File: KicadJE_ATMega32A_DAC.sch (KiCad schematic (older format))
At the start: 72 parts, among them J201 CV1, J202 CV2, J203 OUT1, J204 OUT2, J205 IN1, J206 IN2, P201 Doepfer_Power_16pin, SW201 SW_SPDT, U201 TL072, U202 MCP4822

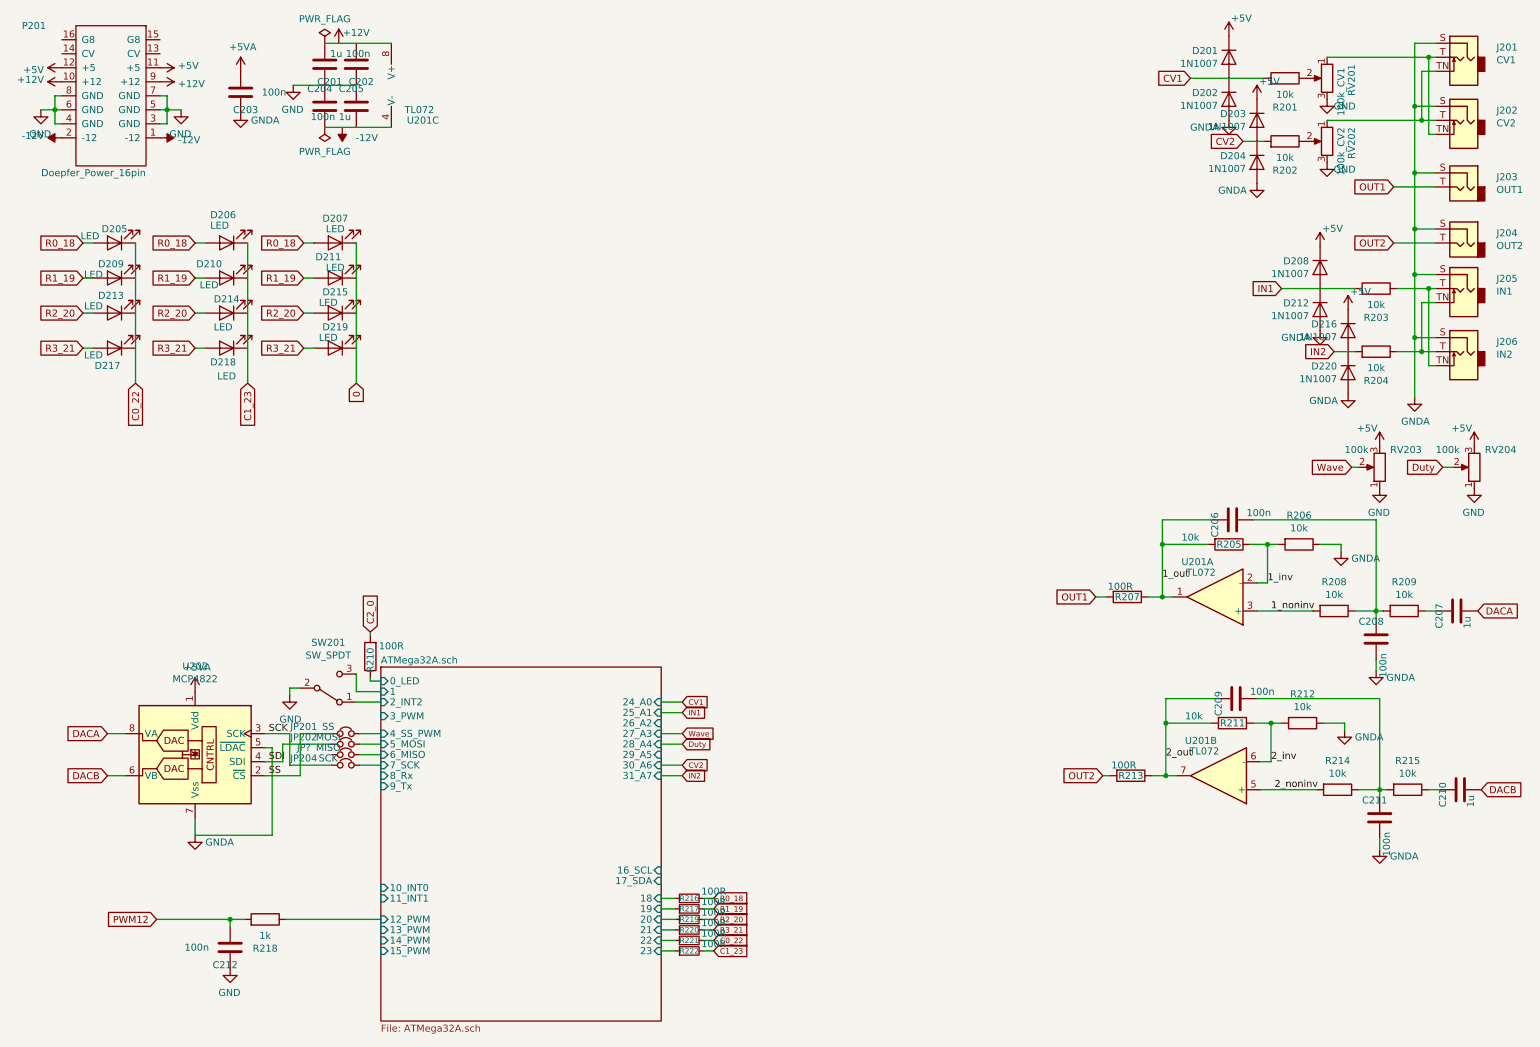
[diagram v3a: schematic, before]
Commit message: Sch cleanup and sorting of components in ATMega
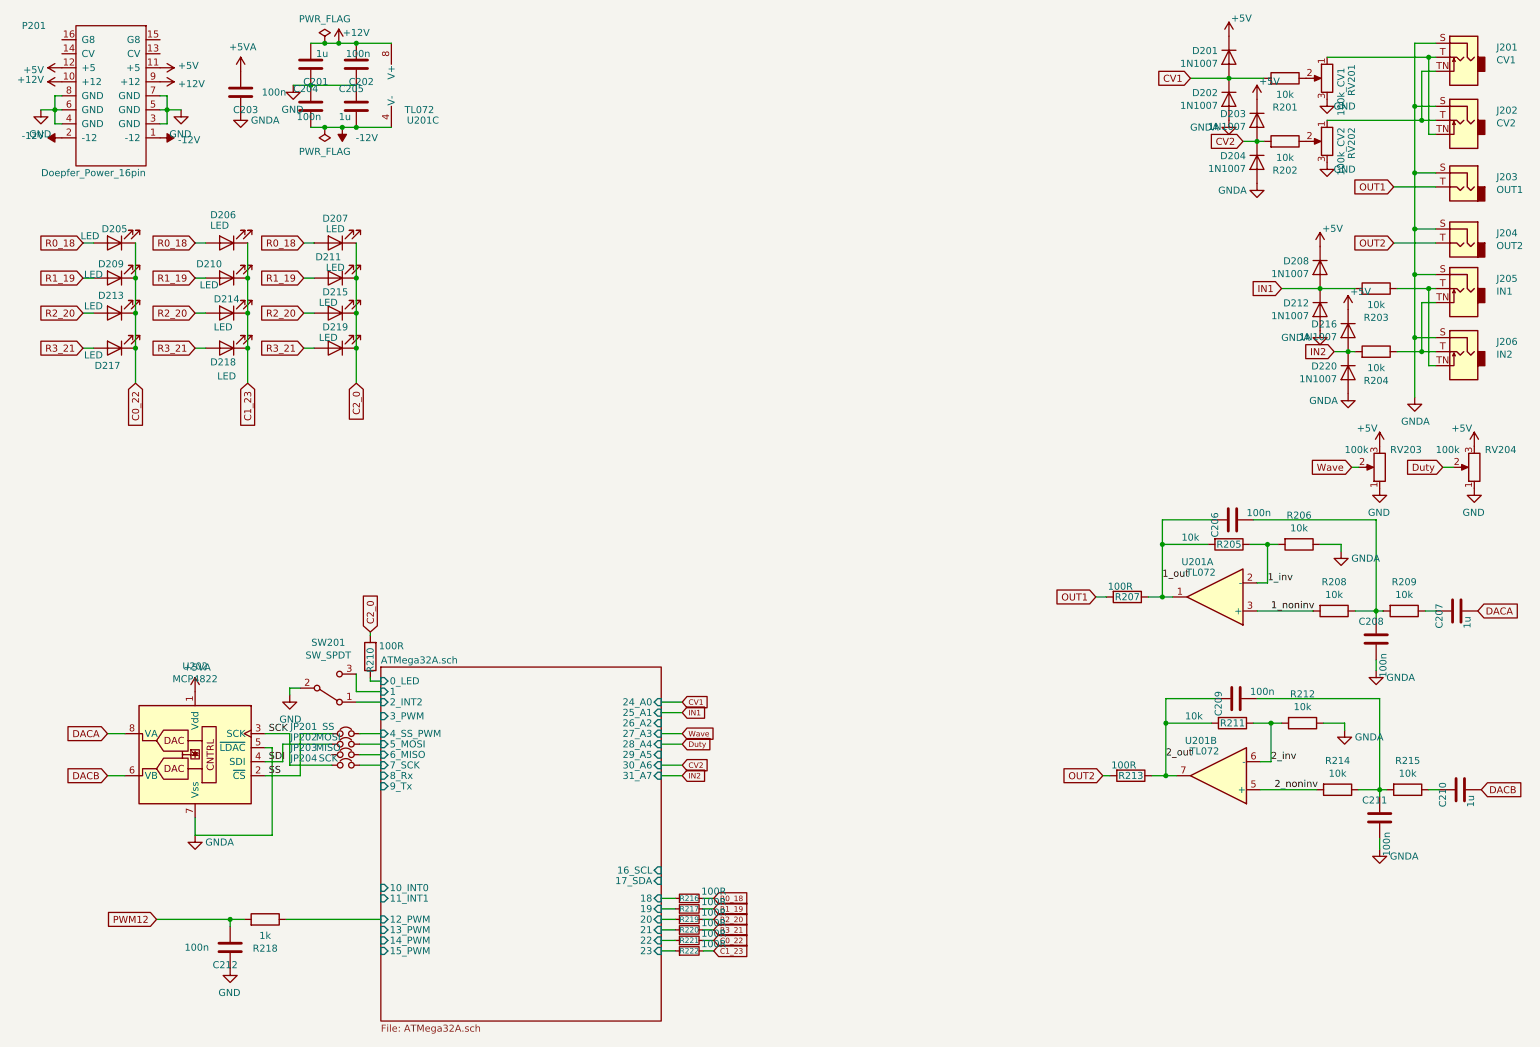
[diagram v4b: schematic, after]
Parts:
- gave numbers to parts that had none: 1
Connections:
- net 0 is gone; now on net C2_0: D207.1 (K)
- net +12V: now also C201.2, C202.2, U201.8 (V+)
- net -12V: now also C204.2, C205.2, U201.4 (V-)
- net C0_22: now also D209.1 (K), D213.1 (K), D217.1 (K)
- net C1_23: now also D210.1 (K), D214.1 (K), D218.1 (K)
- net C2_0: now also D211.1 (K), D215.1 (K), D219.1 (K)
- net CV1: now also D201.2 (A), D202.1 (K)
- net CV2: now also D203.2 (A), D204.1 (K)
- net GND: now also C201.1, C204.1
- net IN1: now also D208.2 (A), D212.1 (K)
- net IN2: now also D216.2 (A), D220.1 (K)
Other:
- moved on the sheet: C201, C204
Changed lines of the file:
@@
 $EndSheet
 Text GLabel 2850 3075 3    50   Input ~ 0
-0
+C2_0
 Wire Wire Line
 	900  2825 975  2825
@@
 L Device:C C?
 U 1 1 5CE712B9
-P 2625 800
+P 2525 800
 AR Path="/5CE712B9" Ref="C?"  Part="1"
 AR Path="/5CD3F059/5CE712B9" Ref="C?"  Part="1"
 AR Path="/5CE3E7A9/5CE712B9" Ref="C201"  Part="1"
-F 0 "C201" H 2500 925 50  0000 L CNN
-F 1 "1u" H 2500 725 50  0000 L CNN
-F 2 "Capacitor_SMD:C_1206_3216Metric_Pad1.42x1.75mm_HandSolder" H 2663 650 50  0001 C CNN
-F 3 "~" H 2625 800 50  0001 C CNN
-	1    2625 800
+F 0 "C201" H 2400 925 50  0000 L CNN
+F 1 "1u" H 2400 725 50  0000 L CNN
+F 2 "Capacitor_SMD:C_1206_3216Metric_Pad1.42x1.75mm_HandSolder" H 2563 650 50  0001 C CNN
+F 3 "~" H 2525 800 50  0001 C CNN
+	1    2525 800
 	-1   0    0    1
 $EndComp
@@
 L Device:C C?
 U 1 1 5CE712D0
-P 2625 1100
+P 2525 1100
 AR Path="/5CE712D0" Ref="C?"  Part="1"
 AR Path="/5CD3F059/5CE712D0" Ref="C?"  Part="1"
 AR Path="/5CE3E7A9/5CE712D0" Ref="C204"  Part="1"
-F 0 "C204" H 2500 1225 50  0000 L CNN
-F 1 "100n" H 2525 1025 50  0000 L CNN
-F 2 "Capacitor_SMD:C_0805_2012Metric_Pad1.15x1.40mm_HandSolder" H 2663 950 50  0001 C CNN
-F 3 "~" H 2625 1100 50  0001 C CNN
-	1    2625 1100
+F 0 "C204" H 2400 1225 50  0000 L CNN
+F 1 "100n" H 2425 1025 50  0000 L CNN
+F 2 "Capacitor_SMD:C_0805_2012Metric_Pad1.15x1.40mm_HandSolder" H 2563 950 50  0001 C CNN
+F 3 "~" H 2525 1100 50  0001 C CNN
+	1    2525 1100
 	1    0    0    -1
 $EndComp
@@
 	1950 6900 1425 6900
 Wire Wire Line
-	8800 900  9325 900
-Wire Wire Line
-	2400 950  2850 950
-Wire Wire Line
-	2625 650  3100 650
-Wire Wire Line
-	2625 1250 3100 1250
-Wire Wire Line
-	9175 1350 9325 1350
-Wire Wire Line
-	9450 2400 9975 2400
-Wire Wire Line
-	9825 2850 9975 2850
-Wire Wire Line
-	1275 2075 1275 3075
-Wire Wire Line
-	2075 2075 2075 3075
-Wire Wire Line
-	2850 2075 2850 3075
+	2400 950  2525 950
+Wire Wire Line
+	2625 1250 2750 1250
+Wire Wire Line
+	1275 2075 1275 2325
+Wire Wire Line
+	2075 2075 2075 2325
+Wire Wire Line
+	2850 2075 2850 2325
 Text Label 9375 4700 0    50   ~ 0
 1_noninv
@@
 SCK
 $Comp
-L Device:Jumper_NC_Small JP?
+L Device:Jumper_NC_Small JP203
 U 1 1 5D23F56B
 P 2775 5725
-F 0 "JP?" H 2475 5775 50  0000 C CNN
+F 0 "JP203" H 2475 5775 50  0000 C CNN
 F 1 "MISO" H 2650 5775 50  0000 C CNN
 F 2 "Connector_PinSocket_2.54mm:PinSocket_1x02_P2.54mm_Vertical" H 2775 5725 50  0001 C CNN
@@
 Text GLabel 5400 6975 2    39   Input ~ 0
 R3_21
+Connection ~ 2525 950
+Wire Wire Line
+	2525 950  2850 950
+Wire Wire Line
+	2525 1250 2625 1250
+Connection ~ 2625 1250
+Connection ~ 2850 1250
+Wire Wire Line
+	2850 1250 3100 1250
+Connection ~ 2750 1250
+Wire Wire Line
+	2750 1250 2850 1250
+Wire Wire Line
+	2625 650  2725 650
+Connection ~ 2850 650
+Wire Wire Line
+	2850 650  3100 650
+Connection ~ 2725 650
+Wire Wire Line
+	2725 650  2850 650
+Wire Wire Line
+	2525 650  2625 650
+Connection ~ 2625 650
+Connection ~ 1275 2325
+Wire Wire Line
+	1275 2325 1275 2575
+Connection ~ 1275 2575
+Wire Wire Line
+	1275 2575 1275 2825
+Connection ~ 1275 2825
+Wire Wire Line
+	1275 2825 1275 3075
+Connection ~ 2075 2325
+Wire Wire Line
+	2075 2325 2075 2575
+Connection ~ 2075 2575
+Wire Wire Line
+	2075 2575 2075 2825
+Connection ~ 2075 2825
+Wire Wire Line
+	2075 2825 2075 3075
+Connection ~ 2850 2325
+Wire Wire Line
+	2850 2325 2850 2575
+Connection ~ 2850 2575
+Wire Wire Line
+	2850 2575 2850 2825
+Connection ~ 2850 2825
+Wire Wire Line
+	2850 2825 2850 3075
+Wire Wire Line
+	9450 2400 9725 2400
+Connection ~ 9725 2400
+Wire Wire Line
+	9725 2400 9975 2400
+Wire Wire Line
+	9825 2850 9925 2850
+Connection ~ 9925 2850
+Wire Wire Line
+	9925 2850 9975 2850
+Wire Wire Line
+	8800 900  9075 900
+Connection ~ 9075 900
+Wire Wire Line
+	9075 900  9325 900
+Wire Wire Line
+	9175 1350 9275 1350
+Connection ~ 9275 1350
+Wire Wire Line
+	9275 1350 9325 1350
 $EndSCHEMATC

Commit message: 12V PWR
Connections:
- net GND: no longer C202.1, C205.1
- net GNDA: now also C202.1, C205.1
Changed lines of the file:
@@
 L power:-12V #PWR?
 U 1 1 5CE712E5
-P 2750 1250
+P 2525 1250
 AR Path="/5CE712E5" Ref="#PWR?"  Part="1"
 AR Path="/5CD3F059/5CE712E5" Ref="#PWR?"  Part="1"
 AR Path="/5CE3E7A9/5CE712E5" Ref="#PWR0215"  Part="1"
-F 0 "#PWR0215" H 2750 1350 50  0001 C CNN
-F 1 "-12V" H 2575 1325 50  0000 C CNN
-F 2 "" H 2750 1250 50  0001 C CNN
-F 3 "" H 2750 1250 50  0001 C CNN
-	1    2750 1250
+F 0 "#PWR0215" H 2525 1350 50  0001 C CNN
+F 1 "-12V" H 2350 1325 50  0000 C CNN
+F 2 "" H 2525 1250 50  0001 C CNN
+F 3 "" H 2525 1250 50  0001 C CNN
+	1    2525 1250
 	-1   0    0    1
 $EndComp
@@
 Wire Wire Line
 	2400 950  2525 950
-Wire Wire Line
-	2625 1250 2750 1250
 Wire Wire Line
 	1275 2075 1275 2325
@@
 Connection ~ 2525 950
 Wire Wire Line
-	2525 950  2850 950
-Wire Wire Line
 	2525 1250 2625 1250
 Connection ~ 2625 1250
@@
 Wire Wire Line
 	2850 1250 3100 1250
-Connection ~ 2750 1250
-Wire Wire Line
-	2750 1250 2850 1250
 Wire Wire Line
 	2625 650  2725 650
@@
 Wire Wire Line
 	9275 1350 9325 1350
+Connection ~ 2525 1250
+Wire Wire Line
+	2625 1250 2850 1250
+$Comp
+L power:GNDA #PWR?
+U 1 1 5D433FC3
+P 2700 950
+AR Path="/5D433FC3" Ref="#PWR?"  Part="1"
+AR Path="/5CD3F059/5D433FC3" Ref="#PWR?"  Part="1"
+AR Path="/5CE3E7A9/5D433FC3" Ref="#PWR?"  Part="1"
+F 0 "#PWR?" H 2700 700 50  0001 C CNN
+F 1 "GNDA" H 2875 900 50  0000 C CNN
+F 2 "" H 2700 950 50  0001 C CNN
+F 3 "" H 2700 950 50  0001 C CNN
+	1    2700 950
+	1    0    0    -1
+$EndComp
+Wire Wire Line
+	2700 950  2850 950
+Connection ~ 2850 950
 $EndSCHEMATC

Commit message: Routed
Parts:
- removed JP203: MISO, Connector_PinSocket_2.54mm:PinSocket_1x02_P2.54mm_Vertical, symbol Device:Jumper_NC_Small
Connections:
- net GND: now also C205.1, D202.2 (A), D204.2 (A); no longer C204.1
- net GNDA: now also C204.1; no longer C205.1, D202.2 (A), D204.2 (A)
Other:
- moved on the sheet: C204, C205
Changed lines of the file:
@@
 	10400 2300 10400 2750
-$Comp
-L power:GNDA #PWR?
-U 1 1 5CDD4247
-P 9075 1200
-AR Path="/5CDD4247" Ref="#PWR?"  Part="1"
-AR Path="/5CD3F059/5CDD4247" Ref="#PWR?"  Part="1"
-AR Path="/5CE3E7A9/5CDD4247" Ref="#PWR0214"  Part="1"
-F 0 "#PWR0214" H 9075 950 50  0001 C CNN
-F 1 "GNDA" H 9250 1150 50  0000 C CNN
-F 2 "" H 9075 1200 50  0001 C CNN
-F 3 "" H 9075 1200 50  0001 C CNN
-	1    9075 1200
-	-1   0    0    -1
-$EndComp
 $Comp
 L Analog_DAC:MCP4822 U202
@@
 L Device:C C?
 U 1 1 5CE712D0
-P 2525 1100
+P 2850 1100
 AR Path="/5CE712D0" Ref="C?"  Part="1"
 AR Path="/5CD3F059/5CE712D0" Ref="C?"  Part="1"
 AR Path="/5CE3E7A9/5CE712D0" Ref="C204"  Part="1"
-F 0 "C204" H 2400 1225 50  0000 L CNN
-F 1 "100n" H 2425 1025 50  0000 L CNN
-F 2 "Capacitor_SMD:C_0805_2012Metric_Pad1.15x1.40mm_HandSolder" H 2563 950 50  0001 C CNN
-F 3 "~" H 2525 1100 50  0001 C CNN
-	1    2525 1100
+F 0 "C204" H 2725 1225 50  0000 L CNN
+F 1 "100n" H 2750 1025 50  0000 L CNN
+F 2 "Capacitor_SMD:C_0805_2012Metric_Pad1.15x1.40mm_HandSolder" H 2888 950 50  0001 C CNN
+F 3 "~" H 2850 1100 50  0001 C CNN
+	1    2850 1100
 	1    0    0    -1
 $EndComp
@@
 L Device:C C?
 U 1 1 5CE712D6
-P 2850 1100
+P 2525 1100
 AR Path="/5CE712D6" Ref="C?"  Part="1"
 AR Path="/5CD3F059/5CE712D6" Ref="C?"  Part="1"
 AR Path="/5CE3E7A9/5CE712D6" Ref="C205"  Part="1"
-F 0 "C205" H 2725 1225 50  0000 L CNN
-F 1 "1u" H 2725 1025 50  0000 L CNN
-F 2 "Capacitor_SMD:C_1206_3216Metric_Pad1.42x1.75mm_HandSolder" H 2888 950 50  0001 C CNN
-F 3 "~" H 2850 1100 50  0001 C CNN
-	1    2850 1100
+F 0 "C205" H 2400 1225 50  0000 L CNN
+F 1 "1u" H 2400 1025 50  0000 L CNN
+F 2 "Capacitor_SMD:C_1206_3216Metric_Pad1.42x1.75mm_HandSolder" H 2563 950 50  0001 C CNN
+F 3 "~" H 2525 1100 50  0001 C CNN
+	1    2525 1100
 	1    0    0    -1
 $EndComp
@@
 	1    9475 1350
 	0    1    -1   0
-$EndComp
-$Comp
-L power:GNDA #PWR?
-U 1 1 5D605339
-P 9275 1650
-AR Path="/5D605339" Ref="#PWR?"  Part="1"
-AR Path="/5CD3F059/5D605339" Ref="#PWR?"  Part="1"
-AR Path="/5CE3E7A9/5D605339" Ref="#PWR0219"  Part="1"
-F 0 "#PWR0219" H 9275 1400 50  0001 C CNN
-F 1 "GNDA" H 9450 1600 50  0000 C CNN
-F 2 "" H 9275 1650 50  0001 C CNN
-F 3 "" H 9275 1650 50  0001 C CNN
-	1    9275 1650
-	-1   0    0    -1
 $EndComp
 $Comp
@@
 Text Label 2225 5575 0    50   ~ 0
 SCK
-$Comp
-L Device:Jumper_NC_Small JP203
-U 1 1 5D23F56B
-P 2775 5725
-F 0 "JP203" H 2475 5775 50  0000 C CNN
-F 1 "MISO" H 2650 5775 50  0000 C CNN
-F 2 "Connector_PinSocket_2.54mm:PinSocket_1x02_P2.54mm_Vertical" H 2775 5725 50  0001 C CNN
-F 3 "~" H 2775 5725 50  0001 C CNN
-	1    2775 5725
-	1    0    0    -1
-$EndComp
-Wire Wire Line
-	2875 5725 3025 5725
 Text GLabel 1700 2075 0    50   Input ~ 0
 R0_18
@@
 Text GLabel 5400 6975 2    39   Input ~ 0
 R3_21
-Connection ~ 2525 950
 Wire Wire Line
 	2525 1250 2625 1250
 Connection ~ 2625 1250
-Connection ~ 2850 1250
-Wire Wire Line
-	2850 1250 3100 1250
 Wire Wire Line
 	2625 650  2725 650
@@
 Wire Wire Line
 	9275 1350 9325 1350
-Connection ~ 2525 1250
-Wire Wire Line
-	2625 1250 2850 1250
 $Comp
 L power:GNDA #PWR?
@@
 AR Path="/5D433FC3" Ref="#PWR?"  Part="1"
 AR Path="/5CD3F059/5D433FC3" Ref="#PWR?"  Part="1"
-AR Path="/5CE3E7A9/5D433FC3" Ref="#PWR?"  Part="1"
-F 0 "#PWR?" H 2700 700 50  0001 C CNN
+AR Path="/5CE3E7A9/5D433FC3" Ref="#PWR0101"  Part="1"
+F 0 "#PWR0101" H 2700 700 50  0001 C CNN
 F 1 "GNDA" H 2875 900 50  0000 C CNN
 F 2 "" H 2700 950 50  0001 C CNN
@@
 Wire Wire Line
 	2700 950  2850 950
+Wire Wire Line
+	2625 1250 2850 1250
 Connection ~ 2850 950
+Connection ~ 2850 1250
+Wire Wire Line
+	2850 1250 3100 1250
+Connection ~ 2525 950
+Connection ~ 2525 1250
+$Comp
+L Envelope-cache-2018-08-04-13-00-04:GND #PWR?
+U 1 1 5D4C4D4B
+P 9275 1650
+F 0 "#PWR?" H 9275 1400 50  0001 C CNN
+F 1 "GND" H 9150 1600 50  0000 C CNN
+F 2 "" H 9275 1650 50  0001 C CNN
+F 3 "" H 9275 1650 50  0001 C CNN
+	1    9275 1650
+	-1   0    0    -1
+$EndComp
+$Comp
+L Envelope-cache-2018-08-04-13-00-04:GND #PWR?
+U 1 1 5D4C4F62
+P 9075 1200
+F 0 "#PWR?" H 9075 950 50  0001 C CNN
+F 1 "GND" H 8950 1150 50  0000 C CNN
+F 2 "" H 9075 1200 50  0001 C CNN
+F 3 "" H 9075 1200 50  0001 C CNN
+	1    9075 1200
+	-1   0    0    -1
+$EndComp
 $EndSCHEMATC

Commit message: ERC Performed
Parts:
- added C213: 100n, Capacitor_SMD:C_0805_2012Metric_Pad1.15x1.40mm_HandSolder, symbol Device:C
- added JP203: PWM1, Jumper:SolderJumper-2_P1.3mm_Open_Pad1.0x1.5mm, symbol Device:Jumper_NC_Small
- added JP205: PWM2, Jumper:SolderJumper-2_P1.3mm_Open_Pad1.0x1.5mm, symbol Device:Jumper_NC_Small
- added R223: 1k, Resistor_SMD:R_0805_2012Metric_Pad1.15x1.40mm_HandSolder, symbol Device:R
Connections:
- net ATMega32A.sch/15_PWM: now also R223.1
- net DACA: now also JP203.2
- net DACB: now also JP205.2
- net GND: now also C213.1
- net PWM12: now also JP203.1
- new net PWM15: C213.2, JP205.1, R223.2
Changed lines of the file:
@@
 U 1 1 5CE0D72D
 P 1700 5675
-F 0 "U202" H 1700 6256 50  0000 C CNN
-F 1 "MCP4822" H 1700 6165 50  0000 C CNN
+F 0 "U202" H 1425 6025 50  0000 C CNN
+F 1 "MCP4822" H 1975 6025 50  0000 C CNN
 F 2 "AJ:AJ_SO-8_5.3x6.2mm_P1.27mm" H 2500 5375 50  0001 C CNN
 F 3 "http://ww1.microchip.com/downloads/en/DeviceDoc/20002249B.pdf" H 2500 5375 50  0001 C CNN
@@
 	-1   0    0    -1
 $EndComp
+$Comp
+L power:PWR_FLAG #FLG?
+U 1 1 5DCE9363
+P 2850 950
+AR Path="/5CD3F059/5DCE9363" Ref="#FLG?"  Part="1"
+AR Path="/5DCE9363" Ref="#FLG?"  Part="1"
+AR Path="/5CE3E7A9/5DCE9363" Ref="#FLG0101"  Part="1"
+F 0 "#FLG0101" H 2850 1025 50  0001 C CNN
+F 1 "PWR_FLAG" H 2850 1123 50  0000 C CNN
+F 2 "" H 2850 950 50  0001 C CNN
+F 3 "~" H 2850 950 50  0001 C CNN
+	1    2850 950
+	0    1    1    0
+$EndComp
+Text GLabel 1400 4075 0    50   Input ~ 0
+PWM12
+$Comp
+L Device:Jumper_NC_Small JP203
+U 1 1 5DCEB6AC
+P 1550 4075
+F 0 "JP203" H 1250 4125 50  0000 C CNN
+F 1 "PWM1" H 1425 4125 50  0000 C CNN
+F 2 "Jumper:SolderJumper-2_P1.3mm_Open_Pad1.0x1.5mm" H 1550 4075 50  0001 C CNN
+F 3 "~" H 1550 4075 50  0001 C CNN
+	1    1550 4075
+	1    0    0    -1
+$EndComp
+Text GLabel 1750 4075 2    50   Input ~ 0
+DACA
+Wire Wire Line
+	1400 4075 1450 4075
+Wire Wire Line
+	1650 4075 1750 4075
+$Comp
+L Device:C C?
+U 1 1 5DD00F28
+P 2500 7325
+AR Path="/5DD00F28" Ref="C?"  Part="1"
+AR Path="/5CD3F059/5DD00F28" Ref="C?"  Part="1"
+AR Path="/5CE3E7A9/5DD00F28" Ref="C213"  Part="1"
+F 0 "C213" H 2375 7450 50  0000 L CNN
+F 1 "100n" H 2175 7325 50  0000 L CNN
+F 2 "Capacitor_SMD:C_0805_2012Metric_Pad1.15x1.40mm_HandSolder" H 2538 7175 50  0001 C CNN
+F 3 "~" H 2500 7325 50  0001 C CNN
+	1    2500 7325
+	1    0    0    1
+$EndComp
+Wire Wire Line
+	2600 7125 2500 7125
+Wire Wire Line
+	2500 7175 2500 7125
+$Comp
+L Device:R R?
+U 1 1 5DD00F35
+P 2750 7125
+AR Path="/5DD00F35" Ref="R?"  Part="1"
+AR Path="/5CD3F059/5DD00F35" Ref="R?"  Part="1"
+AR Path="/5CE3E7A9/5DD00F35" Ref="R223"  Part="1"
+F 0 "R223" V 2543 7125 50  0000 C CNN
+F 1 "1k" V 2634 7125 50  0000 C CNN
+F 2 "Resistor_SMD:R_0805_2012Metric_Pad1.15x1.40mm_HandSolder" V 2680 7125 50  0001 C CNN
+F 3 "~" H 2750 7125 50  0001 C CNN
+	1    2750 7125
+	0    1    -1   0
+$EndComp
+$Comp
+L Envelope-cache-2018-08-04-13-00-04:GND #PWR0108
+U 1 1 5DD00F40
+P 2500 7475
+F 0 "#PWR0108" H 2500 7225 50  0001 C CNN
+F 1 "GND" H 2505 7302 50  0000 C CNN
+F 2 "" H 2500 7475 50  0001 C CNN
+F 3 "" H 2500 7475 50  0001 C CNN
+	1    2500 7475
+	-1   0    0    -1
+$EndComp
+Wire Wire Line
+	2900 7125 3025 7125
+Text GLabel 2500 7125 0    50   Input ~ 0
+PWM15
+Text GLabel 1750 4225 2    50   Input ~ 0
+DACB
+$Comp
+L Device:Jumper_NC_Small JP205
+U 1 1 5DD19CF1
+P 1550 4225
+F 0 "JP205" H 1250 4275 50  0000 C CNN
+F 1 "PWM2" H 1425 4275 50  0000 C CNN
+F 2 "Jumper:SolderJumper-2_P1.3mm_Open_Pad1.0x1.5mm" H 1550 4225 50  0001 C CNN
+F 3 "~" H 1550 4225 50  0001 C CNN
+	1    1550 4225
+	1    0    0    -1
+$EndComp
+Text GLabel 1400 4225 0    50   Input ~ 0
+PWM15
+Wire Wire Line
+	1400 4225 1450 4225
+Wire Wire Line
+	1650 4225 1750 4225
 $EndSCHEMATC
